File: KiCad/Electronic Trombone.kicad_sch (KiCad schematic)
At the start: 25 parts, among them J1 691137710004, J2 691137710003, U1 CD74HC4051E, U2 TL074, U3 TL074

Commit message: started pcb layout
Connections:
- net Trigger 1: now reaches J2.1, U1.11 (S0)
- net Trigger 2: now reaches J2.2, U1.10 (S1)
- net Trigger 3: now reaches J2.3, U1.9 (S2)
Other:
- moved on the sheet: J2
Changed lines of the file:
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@@
 	(wire
 		(pts
-			(xy 149.86 73.66) (xy 149.86 77.47)
+			(xy 157.48 73.66) (xy 157.48 76.2)
 		)
 		(stroke
@@
 	(wire
 		(pts
-			(xy 147.32 73.66) (xy 149.86 73.66)
+			(xy 147.32 73.66) (xy 157.48 73.66)
 		)
 		(stroke
@@
 	(wire
 		(pts
-			(xy 147.32 82.55) (xy 149.86 82.55)
+			(xy 154.94 81.28) (xy 157.48 81.28)
 		)
 		(stroke
@@
 	(wire
 		(pts
-			(xy 147.32 76.2) (xy 148.59 76.2)
+			(xy 147.32 76.2) (xy 156.21 76.2)
 		)
 		(stroke
@@
 	(wire
 		(pts
-			(xy 147.32 78.74) (xy 147.32 82.55)
+			(xy 154.94 78.74) (xy 154.94 81.28)
 		)
 		(stroke
@@
 	(wire
 		(pts
-			(xy 148.59 80.01) (xy 149.86 80.01)
+			(xy 156.21 78.74) (xy 157.48 78.74)
 		)
 		(stroke
@@
 	(wire
 		(pts
+			(xy 154.94 78.74) (xy 147.32 78.74)
+		)
+		(stroke
+			(width 0)
+			(type default)
+		)
+	)
+	(wire
+		(pts
 			(xy 248.92 144.78) (xy 264.16 144.78)
 		)
@@
 	(wire
 		(pts
-			(xy 148.59 76.2) (xy 148.59 80.01)
+			(xy 156.21 76.2) (xy 156.21 78.74)
 		)
 		(stroke
@@
 		)
 	)
+	(label "Trigger 3"
+		(at 147.32 78.74 0)
+		(effects
+			(font
+				(size 1.27 1.27)
+			)
+			(justify left bottom)
+		)
+	)
 	(label "+Pot 2nd Partial"
 		(at 223.52 49.53 0)
@@
 		)
 	)
+	(label "Trigger 2"
+		(at 147.32 76.2 0)
+		(effects
+			(font
+				(size 1.27 1.27)
+			)
+			(justify left bottom)
+		)
+	)
 	(label "In"
 		(at 12.7 172.72 0)
@@
 		)
 	)
+	(label "Trigger 1"
+		(at 147.32 73.66 0)
+		(effects
+			(font
+				(size 1.27 1.27)
+			)
+			(justify left bottom)
+		)
+	)
 	(label "+Pot"
 		(at 60.96 59.69 0)
@@
 	(symbol
 		(lib_id "Header 691137710003:691137710003")
-		(at 154.94 80.01 270)
+		(at 162.56 78.74 270)
 		(unit 1)
 		(body_style 1)
@@
 		(fields_autoplaced yes)
 		(property "Reference" "J2"
-			(at 156.21 80.0099 90)
+			(at 163.83 78.7399 90)
 			(show_name no)
 			(do_not_autoplace no)
@@
 		)
 		(property "Value" "691137710003"
-			(at 156.21 81.2799 90)
+			(at 163.83 80.0099 90)
 			(hide yes)
 			(show_name no)
@@
 		)
 		(property "Footprint" "Header 691137710003:691137710003"
-			(at 154.94 80.01 0)
+			(at 162.56 78.74 0)
 			(hide yes)
 			(show_name no)
@@
 		)
 		(property "Datasheet" ""
-			(at 154.94 80.01 0)
+			(at 162.56 78.74 0)
 			(hide yes)
 			(show_name no)
@@
 		)
 		(property "Description" ""
-			(at 154.94 80.01 0)
+			(at 162.56 78.74 0)
 			(hide yes)
 			(show_name no)

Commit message: added osc core and tuning to pcb layout
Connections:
- net Audio Out: now also J1.1; no longer J1.2
- net Pot Out: now also J1.2; no longer J1.1
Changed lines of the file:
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@@
+		)
+	)
+	(label "Pot Out"
+		(at 24.13 25.4 0)
+		(effects
+			(font
+				(size 1.27 1.27)
+			)
+			(justify left bottom)
 		)
 	)
@@
 		)
 	)
+	(label "Audio Out"
+		(at 24.13 20.32 0)
+		(effects
+			(font
+				(size 1.27 1.27)
+			)
+			(justify left bottom)
+		)
+	)
 	(label "+Pot 4th Partial"
 		(at 74.93 60.96 0)
@@
 		)
 	)
-	(label "Pot Out"
-		(at 24.13 20.32 0)
-		(effects
-			(font
-				(size 1.27 1.27)
-			)
-			(justify left bottom)
-		)
-	)
 	(label "+Pot 3rd Partial"
 		(at 149.86 71.12 0)
@@
 		(effects
 			(font
-				(size 1.27 1.27)
-			)
-			(justify left bottom)
-		)
-	)
-	(label "Audio Out"
-		(at 24.13 25.4 0)
-		(effects
-			(font

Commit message: minor but important changes to schematic
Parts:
- added R75, R76: R_US, Resistor_THT:R_Axial_DIN0207_L6.3mm_D2.5mm_P7.62mm_Horizontal, symbol Device:R_US
- renumbered U2 to U11
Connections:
- net +5V: now also R76.2
- net Amplifier/Out: now also U2.5 (+); no longer U2.10 (+)
- net Audio Out: now also U2.8, U2.9 (-); no longer U2.13 (-), U2.14
- net GND: now also R75.1
- net Pot Voltage Difference: now also R75.2, R76.1
- net at RV8.2: now also U2.10 (+); no longer U2.12 (+)
- net at R5.2, RV8.1: now also U2.7; no longer U2.8
- net at R5.1, R6.2: now also U2.6 (-); no longer U2.9 (-)

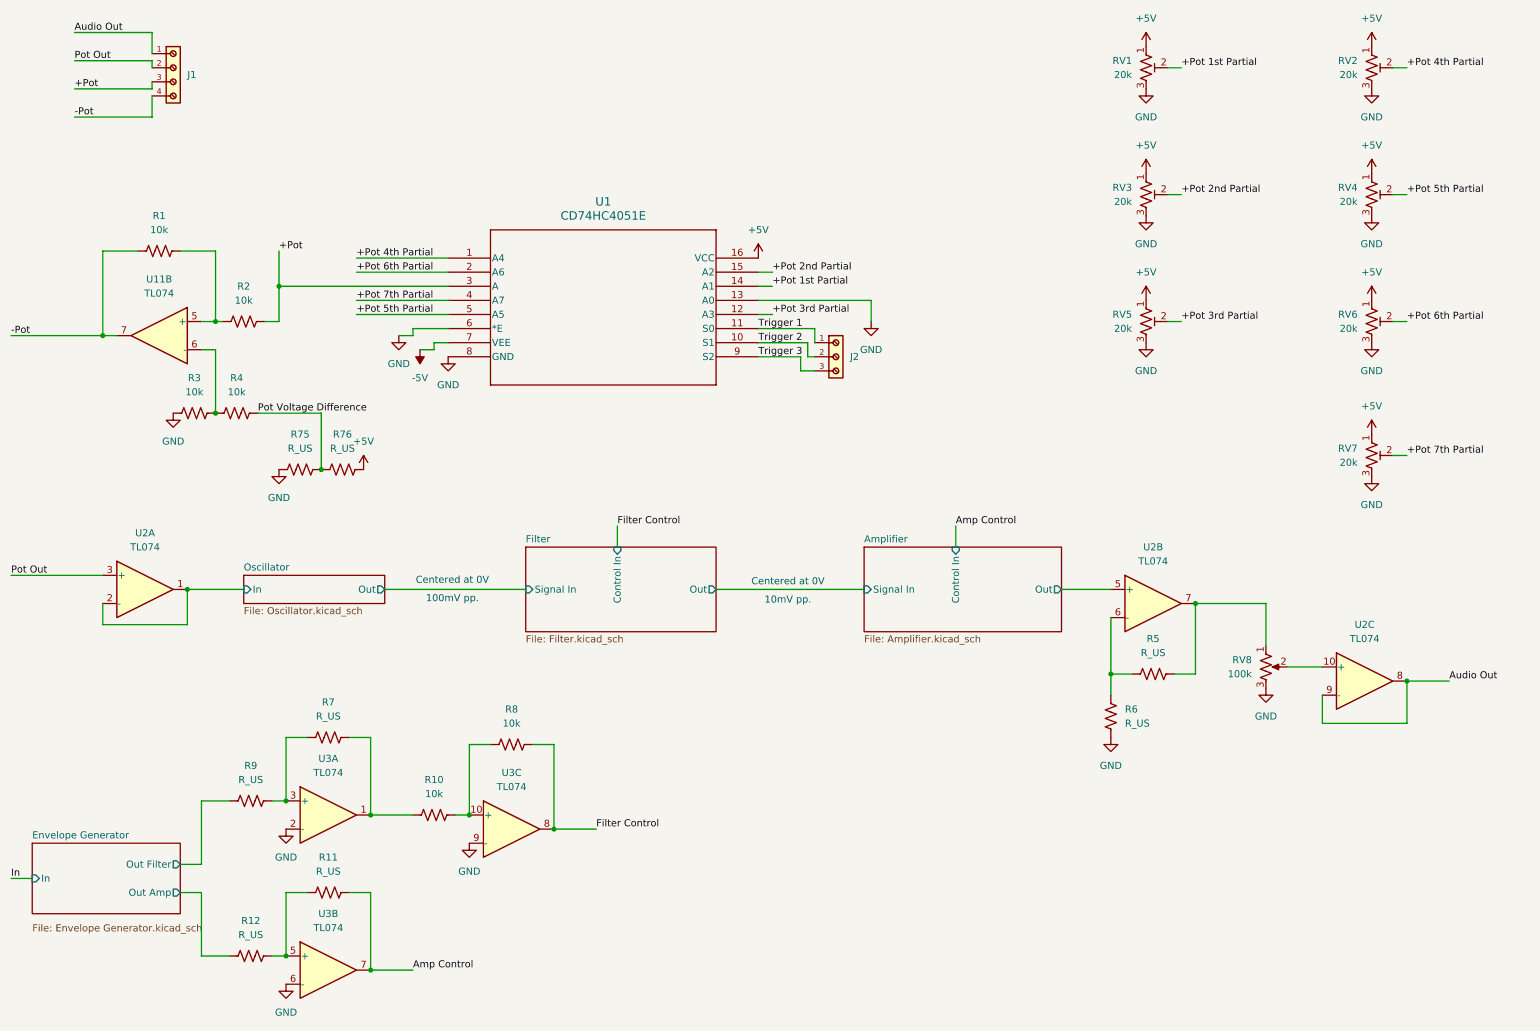
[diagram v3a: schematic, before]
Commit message: fixed custom pot voltage control schematic
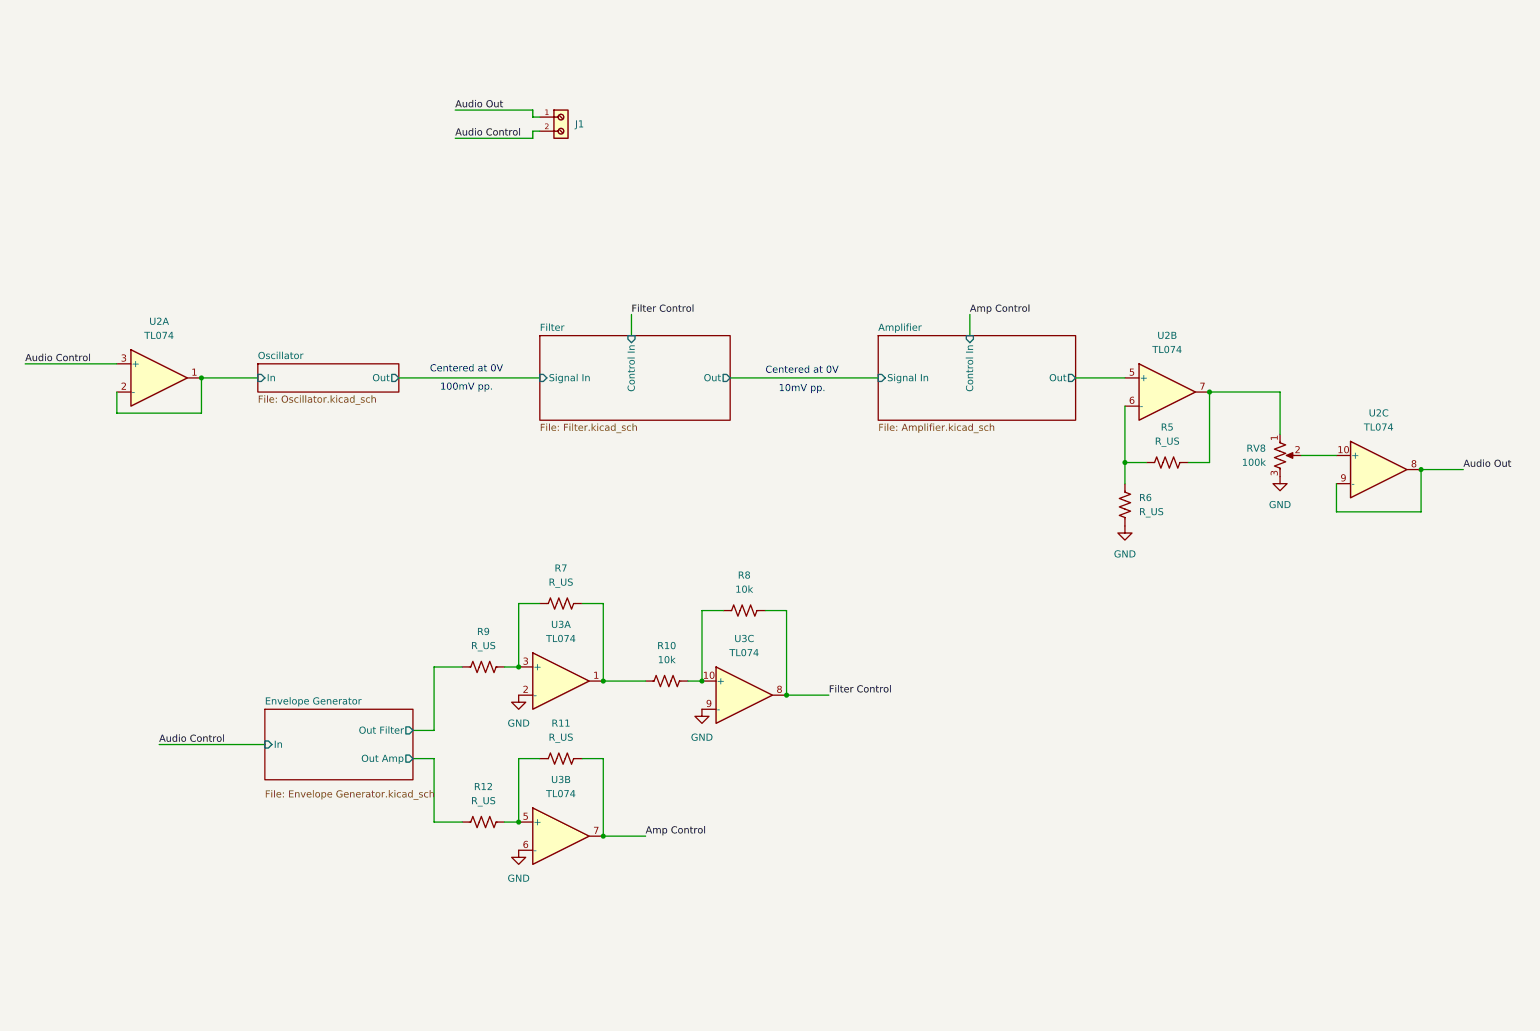
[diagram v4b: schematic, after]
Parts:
- removed J1: 691137710004, Header 691137710004:691137710004, symbol Header 691137710004:691137710004
- removed J2: 691137710003, Header 691137710003:691137710003, symbol Header 691137710003:691137710003
- removed R1, R2, R3, R4: 10k, Resistor_SMD:R_0201_0603Metric, symbol Device:R_US
- removed R75, R76: R_US, Resistor_THT:R_Axial_DIN0207_L6.3mm_D2.5mm_P7.62mm_Horizontal, symbol Device:R_US
- removed RV1, RV2, RV3, RV4, RV5, RV6, RV7: 20k, Potentiometer_SMD:Potentiometer_Bourns_TC33X_Vertical, symbol Device:R_Potentiometer_Trim_US
- removed U1: CD74HC4051E, Mux CD74HC4051E:N16, symbol Mux CD74HC4051E:CD74HC4051E
- removed U11: TL074, Package_DIP:DIP-14_W7.62mm, symbol Amplifier_Operational:TL074
- added J1: 691137710002, Header 691137710002:691137710002, symbol Header 691137710002:691137710002
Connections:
- net Audio Out: now also J1.1
- net Pot Out renamed Audio Control
- net Audio Control: now also J1.2
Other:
- moved on the sheet: R10, R11, R12, R5, R6, R7, R8, R9, RV8, U2A, U2B, U2C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
